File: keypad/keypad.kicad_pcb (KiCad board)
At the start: 2 copper layers, 50 x 50 mm, 55 parts, among them P1 USB_C_Plug_USB2.0, SW1 SW_MEC_5E, SW2 SW_MEC_5E, SW3 SW_DIP_x01, SW4 SW_Push, SW5 SW_Push, SW6 SW_Push, U1 RP2040, U2 74HCT245, U3 W25Q16JVUXIQ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

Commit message: Finish RGB and start power
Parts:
- removed SW6: SW_Push, Button_Switch_Keyboard:SW_Cherry_MX_1.00u_PCB
- removed U7: DRV5033AJxDBZ, Package_TO_SOT_SMD:SOT-23
- added D7: WS2812B, LED_SMD:LED_WS2812B_PLCC4_5.0x5.0mm_P3.2mm, F.Cu at (87.5, 70.7)
- added D8: WS2812B, LED_SMD:LED_WS2812B_PLCC4_5.0x5.0mm_P3.2mm, F.Cu at (126.5, 70.7)
- added D9: WS2812B, LED_SMD:LED_WS2812B_PLCC4_5.0x5.0mm_P3.2mm, F.Cu at (126.5, 111.2)
- C10, C11, C21, C5, C6, C7, D1, D2, D3, D4, U2: moved to B.Cu
- C3, C4: value 27 pF -> 10 pF
- SW1, SW2: footprint Button_Switch_THT:SW_Push_2P1T_Toggle_CK_PVA1xxH1xxxxxxV2 -> Button_Switch_SMD:SW_Push_1P1T_NO_6x6mm_H9.5mm
- SW3: footprint Button_Switch_SMD:SW_DIP_SPSTx01_Slide_9.78x4.72mm_W8.61mm_P2.54mm -> Jumper:SolderJumper-2_P1.3mm_Open_Pad1.0x1.5mm
- Y1: value ABLS-12.000MHz-B4-T -> ABM8G-12.000MHZ-4Y-T3; footprint Crystal:Crystal_HC18-U_Vertical -> Crystal:Crystal_SMD_Abracon_ABM8G-4Pin_3.2x2.5mm
- moved D5 100.3 mm to (87.4, 111.2)
- moved C11 93.5 mm to (100.4, 110.8), turned to 180 degrees
- moved R8 87.6 mm to (88.0, 98.7)
- moved U6 86.8 mm to (87.2, 81.0), turned to -90 degrees
- moved C5 84.9 mm to (100.4, 106.0), turned to 180 degrees
- moved SW4 82.6 mm to (99.4, 76.0)
- moved D3 78.6 mm to (87.5, 70.7), turned to 180 degrees
- moved D4 77.9 mm to (87.4, 111.2), turned to 180 degrees
- moved R5 75.3 mm to (115.8, 110.0), turned to 180 degrees
- moved C6 71.3 mm to (100.4, 108.4), turned to 180 degrees
- moved C7 63.6 mm to (101.0, 103.0), turned to 90 degrees
- moved U2 63.2 mm to (118.2, 110.3)
- moved SW5 60.3 mm to (119.5, 76.0)
- moved U5 56.9 mm to (126.8, 81.0), turned to -90 degrees
- moved C21 55.2 mm to (113.0, 106.0), turned to 90 degrees
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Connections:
- C21 pad 1: +3.3V -> Net-(C5-Pad1)
- D5 pad 2: unconnected-(D5-Pad2) -> Net-(D5-Pad2)
- SW1 pad 2: unconnected-(SW1-Pad2) -> +3.3V
- SW2 pad 2: unconnected-(SW2-Pad2) -> +3.3V
- U1 pad 12: RGB_D0 -> unconnected-(U1-Pad12)
- U1 pad 28: unconnected-(U1-Pad28) -> RGB_D0
- U1 pad 29: unconnected-(U1-Pad29) -> AUX0
- U1 pad 30: unconnected-(U1-Pad30) -> AUX1
- U1 pad 40: ADC2 -> unconnected-(U1-Pad40)
- U1 pad 6: AUX0 -> unconnected-(U1-Pad6)
- U1 pad 7: AUX1 -> unconnected-(U1-Pad7)
- Y1 pad 2: Net-(C3-Pad2) -> GND
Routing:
- net ADC0: track 0.00 -> 44.8 mm
- net Net-(D5-Pad2): track 0.00 -> 41.4 mm
- net Net-(D1-Pad2): track 0.00 -> 41.4 mm
- net Net-(D8-Pad2): track 0.00 -> 40.1 mm
- net Net-(D7-Pad2): track 0.00 -> 39.9 mm, vias 0 -> 2
- net Net-(D2-Pad2): track 0.00 -> 39.7 mm
- net Net-(D3-Pad2): track 0.00 -> 39.5 mm
- net ADC1: track 0.00 -> 37.0 mm, vias 0 -> 2
- net +3.3V: track 0.00 -> 27.2 mm, vias 0 -> 3
- net GND: track 0.00 -> 26.7 mm
- net Net-(C5-Pad1): track 0.00 -> 20.4 mm, vias 0 -> 2
- net USB_DN: track 29.3 -> 47.4 mm
- net USB_DP: track 34.9 -> 52.0 mm
- net QSPI_SS: track 15.6 -> 31.1 mm
- net QSPI_SD1: track 14.6 -> 25.4 mm
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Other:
- board size 50 x 50 mm -> 50 x 58.2 mm

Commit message: finish placing everything
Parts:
- added C22: 100n, Capacitor_SMD:C_0805_2012Metric, B.Cu at (112.6, 111.0)
- added J1: Conn_01x02_Male, Connector_PinHeader_1.27mm:PinHeader_1x02_P1.27mm_Vertical, F.Cu at (87.6, 92.8)
- C1, C12, C14, C17, C18, C2, C8, D6, R1, R2, R3, R4, U4: moved to B.Cu
- moved R12 103.9 mm to (95.6, 97.8)
- moved C20 92.7 mm to (87.2, 77.8), turned to 180 degrees
- moved C13 86.4 mm to (93.4, 72.6)
- moved R3 86.3 mm to (112.0, 92.2)
- moved C18 81.8 mm to (97.8, 94.0), turned to -90 degrees
- moved R10 80.2 mm to (103.2, 72.2), turned to -90 degrees
- moved C15 80.0 mm to (93.4, 70.4)
- moved C1 79.0 mm to (116.0, 94.8)
- moved R11 78.8 mm to (92.0, 97.8)
- moved R9 78.4 mm to (101.0, 72.2), turned to -90 degrees
- moved R13 76.1 mm to (99.2, 97.8)
- moved R2 75.1 mm to (123.2, 94.8), turned to 180 degrees
- moved R1 72.1 mm to (112.0, 94.8), turned to 180 degrees
- moved C4 72.0 mm to (119.0, 106.4), turned to -90 degrees
- moved C16 71.2 mm to (99.4, 100.4)
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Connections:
- C7 pad 1: +3.3V -> ADC_AVDD
- U1 pad 24: unconnected-(U1-Pad24) -> Net-(U1-Pad24)
- U1 pad 25: unconnected-(U1-Pad25) -> Net-(U1-Pad25)
- U1 pad 43: +3.3V -> ADC_AVDD
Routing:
- net +3.3V: track 27.2 -> 215.2 mm, vias 3 -> 9
- net VBUS: track 2.26 -> 181.3 mm, vias 0 -> 6
- net Net-(U1-Pad24): track 0.00 -> 44.6 mm, vias 0 -> 1
- net Net-(U1-Pad25): track 0.00 -> 42.1 mm, vias 0 -> 1
- net ADC_AVDD: track 0.00 -> 23.3 mm, vias 0 -> 2
- net AUX1: track 0.00 -> 21.6 mm, vias 0 -> 1
- net GND: track 26.7 -> 42.7 mm, vias 0 -> 4
- net AUX0: track 0.00 -> 14.5 mm, vias 0 -> 1
- net Net-(R2-Pad2): track 0.00 -> 14.4 mm, vias 0 -> 1
- net Net-(R1-Pad2): track 0.00 -> 14.3 mm, vias 0 -> 1
- net Net-(C17-Pad1): track 0.00 -> 14.0 mm
- net Net-(P1-PadB5): track 0.00 -> 11.5 mm, vias 0 -> 1
- net Net-(C3-Pad2): track 7.91 -> 16.9 mm
- net Net-(P1-PadA5): track 0.00 -> 8.33 mm, vias 0 -> 2
- net RGB_D0: track 5.59 -> 9.96 mm
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- added copper zone on B.Cu, net GND
- added copper zone on F.Cu, net GND

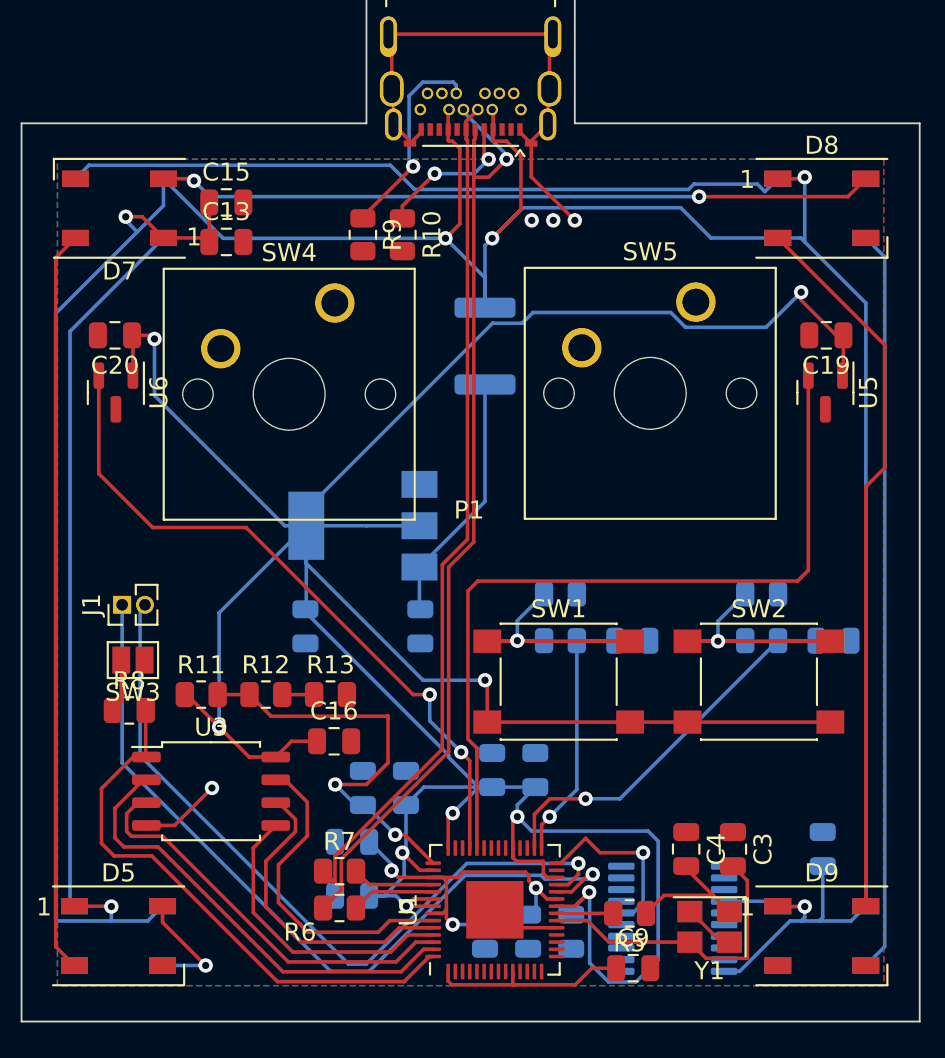
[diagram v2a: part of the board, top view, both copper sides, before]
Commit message: fix all the disconnected GND problems
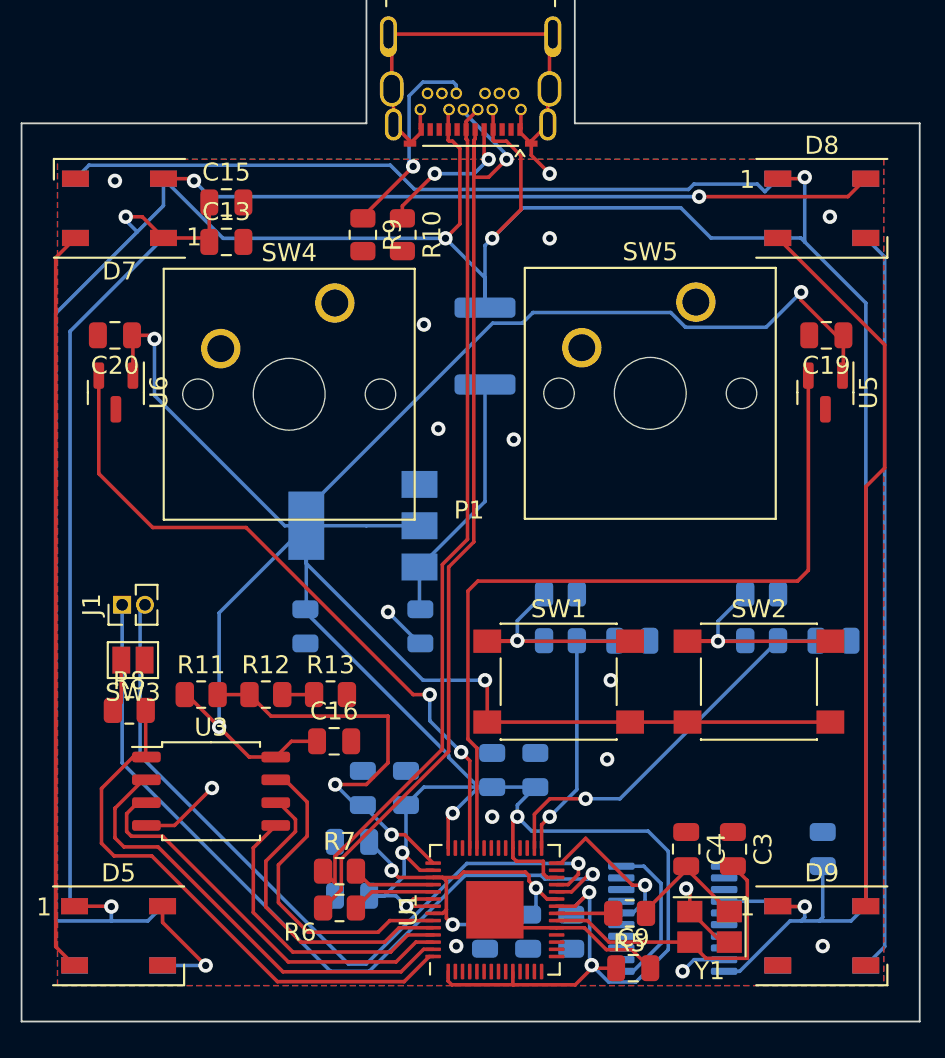
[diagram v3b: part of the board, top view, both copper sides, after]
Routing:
- net GND: track 42.7 -> 63.1 mm, vias 4 -> 16
- net Net-(C4-Pad2): track 8.95 -> 6.95 mm
- net RGB_D0: track 9.96 -> 9.05 mm
- net +3.3V: track 215.2 -> 215.7 mm, vias 9 -> 10

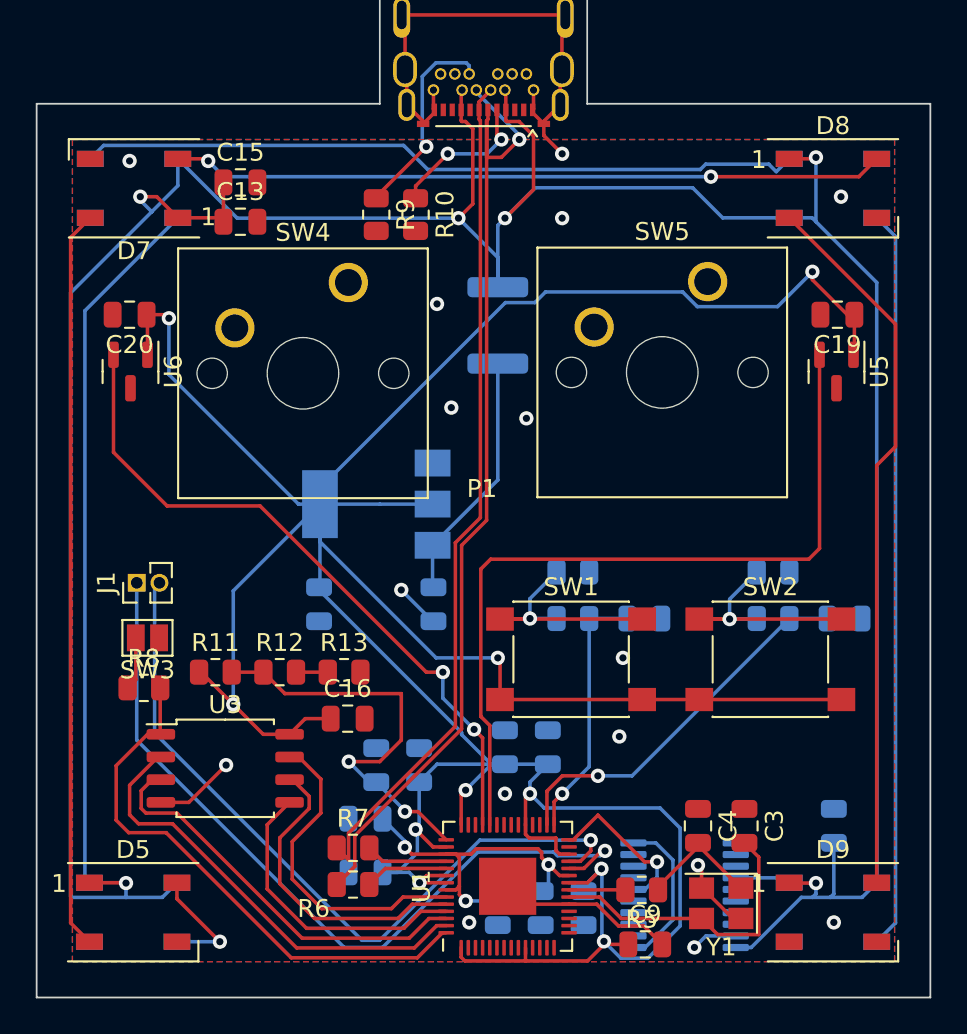
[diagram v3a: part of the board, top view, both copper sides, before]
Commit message: Rewire RGB to add space for screwholes
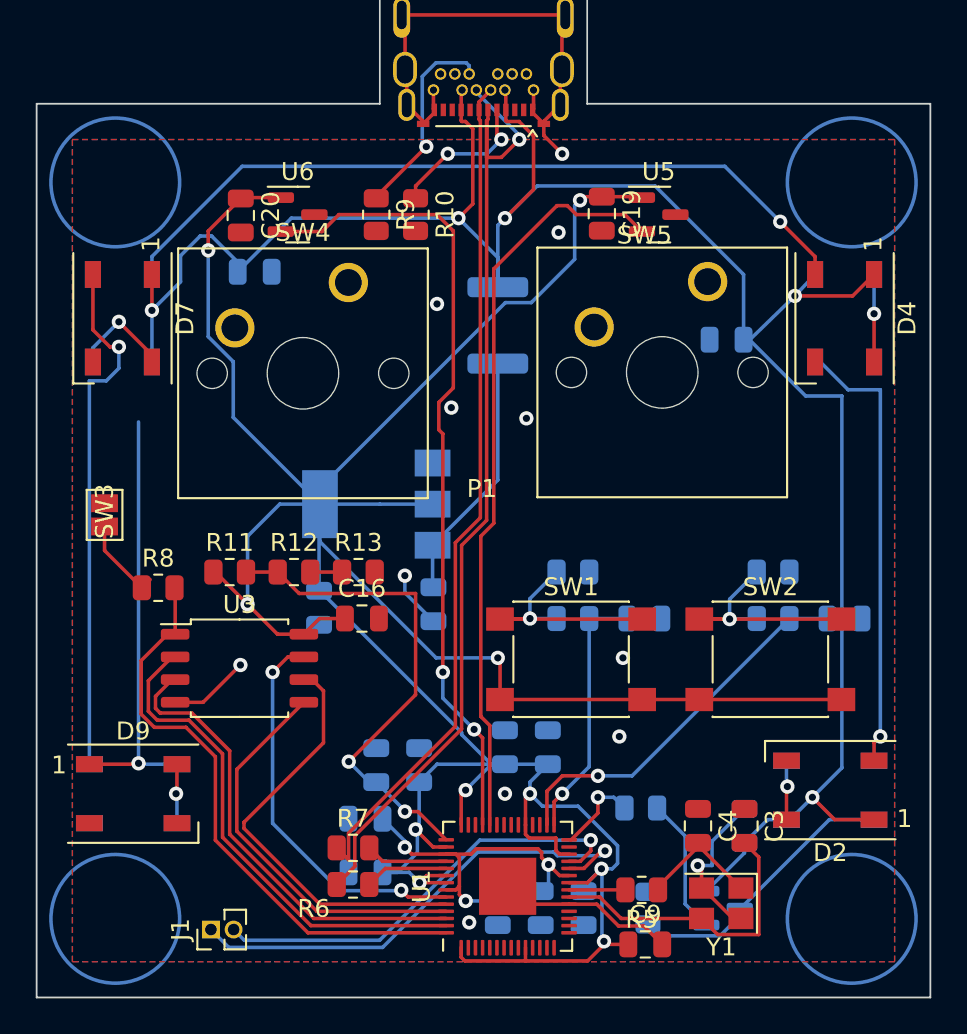
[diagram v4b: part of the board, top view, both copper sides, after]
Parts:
- removed U2: 74HCT245, Package_SO:TSSOP-20_4.4x6.5mm_P0.65mm
- added Q1: BC807, Package_TO_SOT_SMD:SOT-23, B.Cu at (120.4, 111.0)
- added R14: 1K, Resistor_SMD:R_0805_2012Metric, B.Cu at (115.8, 105.4)
- added R15: 10K, Resistor_SMD:R_0805_2012Metric, B.Cu at (116.2, 111.0)
- C13: value 10u -> 100n; moved to B.Cu
- C15, D5, D8: moved to B.Cu
- D2, D4: moved to F.Cu
- moved D4 51.8 mm to (127.2, 78.0), turned to -90 degrees
- moved D8 51.8 mm to (87.4, 104.6), turned to 180 degrees
- moved D3 40.4 mm to (127.2, 78.0), turned to -90 degrees
- moved D9 39.7 mm to (87.4, 104.6)
- moved D2 33.7 mm to (126.4, 104.4), turned to 180 degrees
- moved D5 33.2 mm to (86.8, 78.0), turned to 90 degrees
- moved C15 28.6 mm to (120.6, 79.2), turned to 180 degrees
- moved J1 19.8 mm to (91.8, 112.2)
- moved C19 14.3 mm to (113.6, 72.2), turned to -90 degrees
- moved U5 13.3 mm to (116.8, 72.2), turned to 0 degrees
- moved U6 12.8 mm to (96.6, 72.2), turned to 0 degrees
- moved C20 8.34 mm to (93.4, 72.2), turned to -90 degrees
- moved D7 7.30 mm to (86.8, 78.0), turned to -90 degrees
- moved SW3 7.29 mm to (85.8, 89.0), turned to -90 degrees
- moved D1 6.83 mm to (126.4, 104.4), turned to 0 degrees
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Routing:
- net Net-(D1-Pad2): track 41.4 -> 3.34 mm, vias 0 -> 1
- net Net-(D8-Pad2): track 40.1 -> 3.34 mm, vias 0 -> 1
- net Net-(D4-Pad2): track 6.69 -> 43.3 mm
- net Net-(D5-Pad2): track 41.4 -> 5.87 mm, vias 0 -> 1
- net Net-(D3-Pad2): track 39.5 -> 4.97 mm, vias 0 -> 1
- net VBUS: track 181.3 -> 149.3 mm
- net +3.3V: track 215.7 -> 191.0 mm
- net Net-(J1-Pad2): track 42.1 -> 24.6 mm
- net Net-(J1-Pad1): track 44.6 -> 27.3 mm
- net Net-(D2-Pad2): track 40.6 -> 25.2 mm, vias 0 -> 1
- net Net-(D1-Pad4): track 3.14 -> 15.9 mm
- net Net-(D7-Pad2): track 40.3 -> 29.5 mm, vias 2 -> 1
- net Net-(Q1-Pad1): track 0.00 -> 7.69 mm
- net ADC1: track 38.4 -> 45.0 mm
- net QSPI_SCLK: track 17.5 -> 24.0 mm
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
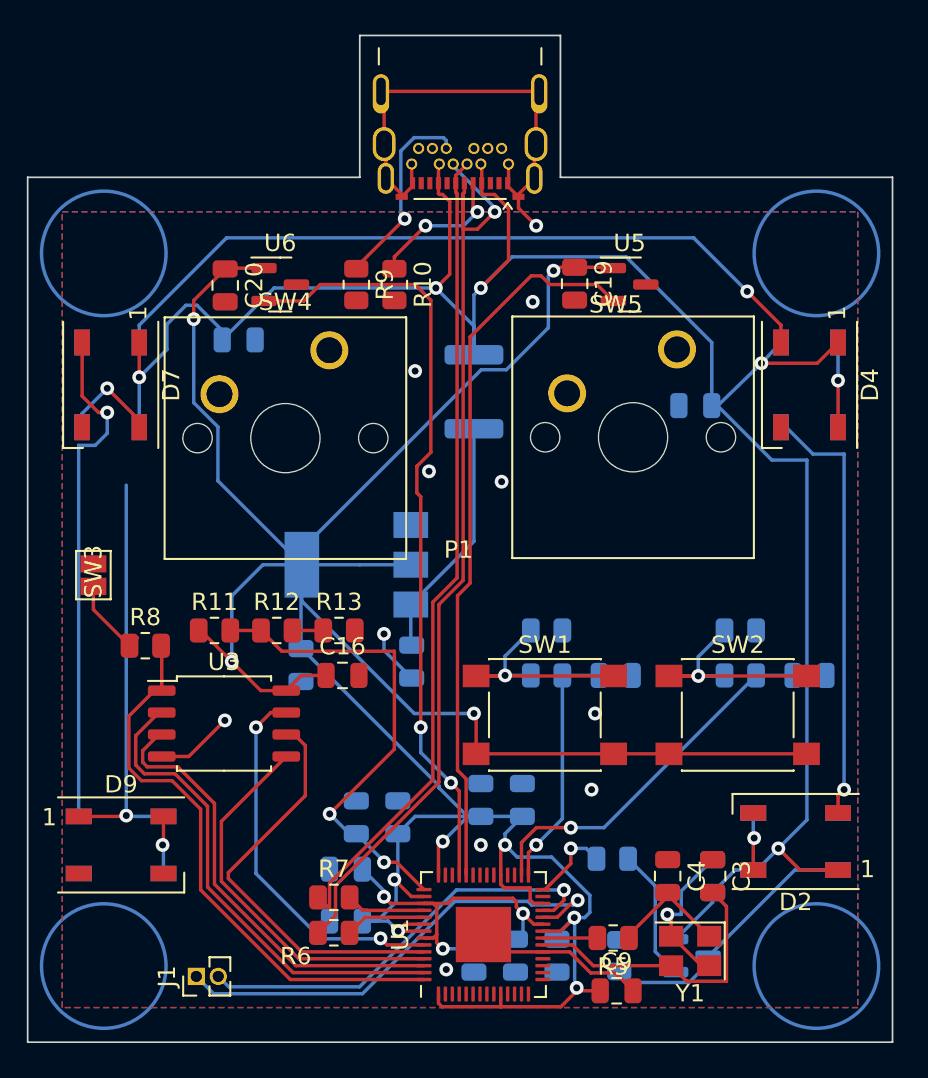
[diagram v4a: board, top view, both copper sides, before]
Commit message: Re-spec USB-C and power diode
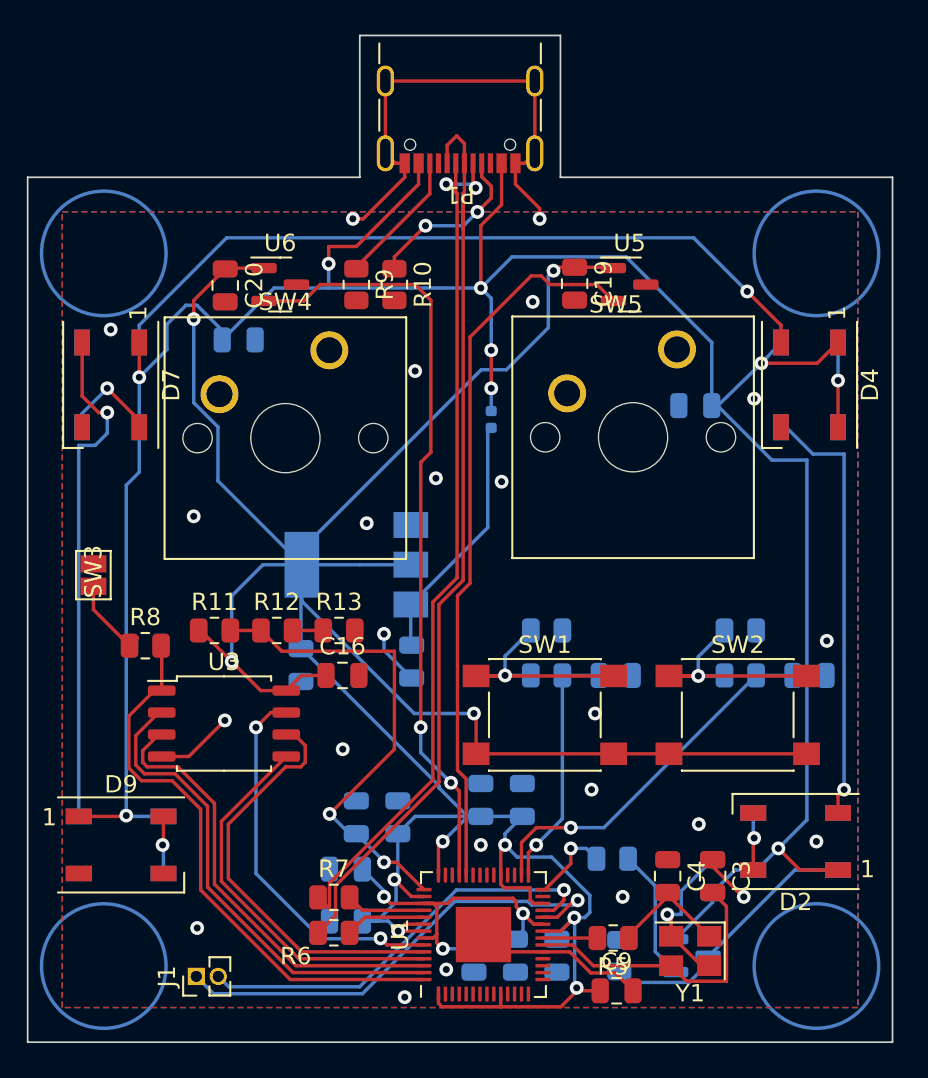
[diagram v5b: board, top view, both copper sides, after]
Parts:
- D6: value D_Schottky -> RB161QS-40; footprint Diode_SMD:D_1812_4532Metric -> Diode_SMD:D_0402_1005Metric
- P1: value USB_C_Plug_USB2.0 -> USB4105-GF-A; footprint Connector_USB:USB_C_Receptacle_CNCTech_C-ARA1-AK51X -> Connector_USB:USB_C_Receptacle_GCT_USB4105-xx-A_16P_TopMnt_Horizontal
- moved D6 1.89 mm to (108.8, 80.0)
- moved P1 1.52 mm to (107.0, 61.5)
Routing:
- net VBUS: track 149.3 -> 155.3 mm, vias 6 -> 8
- net Net-(P1-PadB5): track 11.5 -> 7.86 mm, vias 1 -> 0
- net USB_DN: track 47.4 -> 51.0 mm, vias 0 -> 2
- net Net-(P1-PadA5): track 8.33 -> 10.2 mm
- net USB_DP: track 54.9 -> 53.6 mm, vias 1 -> 0
- net GND: track 57.2 -> 57.9 mm, vias 12 -> 25
- net QSPI_SCLK: track 24.0 -> 24.5 mm

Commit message: Minor updates, prep for fab
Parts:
- removed C1, C2: 10u, Capacitor_SMD:C_0805_2012Metric
- removed R1, R2: 100R, Resistor_SMD:R_0805_2012Metric
- added REF**: MountingHole_5.3mm_M5, MountingHole:MountingHole_5.3mm_M5, F.Cu at (86.4, 111.6)
- added REF**: MountingHole_5.3mm_M5, MountingHole:MountingHole_5.3mm_M5, F.Cu at (86.4, 70.4)
- added REF**: MountingHole_5.3mm_M5, MountingHole:MountingHole_5.3mm_M5, F.Cu at (127.6, 111.6)
- added REF**: MountingHole_5.3mm_M5, MountingHole:MountingHole_5.3mm_M5, F.Cu at (127.6, 70.4)
- D1, D2, D3, D4, D5, D7, D8, D9: value WS2812B -> WS2812B-B/T
- J1: value Conn_01x02_Male -> NO FIT
- Q1: value BC807 -> BC807-40LT1G
- R3, R4: moved to F.Cu
- SW1, SW2: value SW_MEC_5E -> TS04-66-70-BK-100-SMT
- SW3: value SW_DIP_x01 -> NO FIT
- SW4, SW5: value SW_Push -> NO FIT
- U3: value W25Q16JVUXIQ -> W25Q16JVSSIQ
- U5, U6: value DRV5033AJxDBZ -> DRV5053VAQDBZR
- moved R3 3.03 mm to (115.0, 92.6), turned to 180 degrees
- moved R4 2.83 mm to (126.0, 92.6), turned to 180 degrees
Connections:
- R3 pad 1: Net-(R1-Pad2) -> AUX0
- R4 pad 1: Net-(R2-Pad2) -> AUX1
- SW1 pad 1: Net-(R1-Pad2) -> AUX0
- SW2 pad 1: Net-(R2-Pad2) -> AUX1
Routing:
- net Net-(R2-Pad2): track 14.4 -> 0.00 mm, vias 1 -> 0
- net Net-(R1-Pad2): track 14.3 -> 0.00 mm, vias 1 -> 0
- net AUX0: track 14.5 -> 27.5 mm, vias 1 -> 2
- net AUX1: track 21.6 -> 32.9 mm, vias 1 -> 2
- net ADC1: track 44.8 -> 45.4 mm

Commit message: fix mistakes because i am big dum
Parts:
- C3, C4: value 10 pF -> 2p
- P1: value USB4105-GF-A -> GT-USB-7010ASV; footprint Connector_USB:USB_C_Receptacle_GCT_USB4105-xx-A_16P_TopMnt_Horizontal -> Connector_USB:USB_C_Receptacle_G-Switch_GT-USB-7010ASV
- Y1: value ABM8G-12.000MHZ-4Y-T3 -> NX3225SA-12MHz-STD-CSR-6; footprint Crystal:Crystal_SMD_Abracon_ABM8G-4Pin_3.2x2.5mm -> Crystal:Crystal_SMD_3225-4Pin_3.2x2.5mm
- moved C15 0.99 mm to (121.3, 78.5)
- moved SW4 0.56 mm to (100.0, 76.0)
- moved SW5 0.54 mm to (119.0, 76.0)
- moved Y1 0.29 mm to (120.4, 111.0), turned to 0 degrees
- moved P1 0.11 mm to (107.0, 61.4)
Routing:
- net VBUS: track 155.3 -> 154.1 mm
- net Net-(C3-Pad2): track 16.9 -> 18.1 mm
- net +3.3V: track 191.0 -> 191.7 mm
- net Net-(R8-Pad1): track 4.95 -> 4.29 mm
- net USB_DN: track 51.0 -> 51.6 mm
